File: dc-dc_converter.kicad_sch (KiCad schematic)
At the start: 11 parts

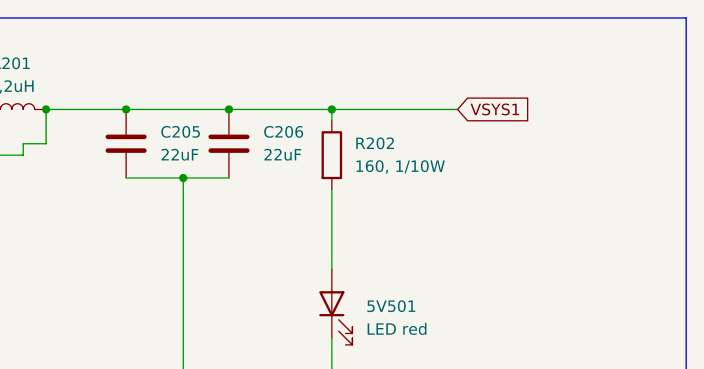
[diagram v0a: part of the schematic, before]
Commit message: daughterboard created
divided into mainboard and daughterboard
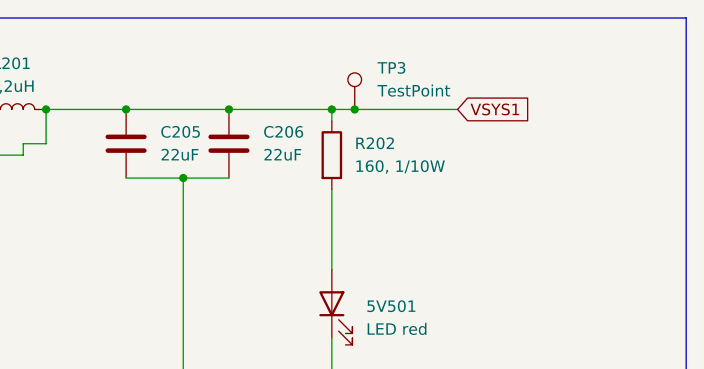
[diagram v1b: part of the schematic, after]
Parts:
- added TP3: TestPoint, TestPoint:TestPoint_Pad_D1.0mm, symbol Connector:TestPoint
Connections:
- net VSYS1: now also TP3.1
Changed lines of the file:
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@@
+	)
+	(junction
+		(at 200.66 39.37)
+		(diameter 0)
+		(color 0 0 0 0)
 	)
 	(junction
@@
 	(wire
 		(pts
+			(xy 200.66 39.37) (xy 212.09 39.37)
+		)
+		(stroke
+			(width 0)
+			(type default)
+		)
+	)
+	(wire
+		(pts
 			(xy 163.83 43.18) (xy 166.37 43.18)
 		)
@@
 	(wire
 		(pts
-			(xy 198.12 39.37) (xy 212.09 39.37)
+			(xy 198.12 39.37) (xy 200.66 39.37)
 		)
 		(stroke
@@
 					(unit 1)
 				)
+			)
+		)
+	)
+	(symbol
+		(lib_id "Connector:TestPoint")
+		(at 200.66 39.37 0)
+		(unit 1)
+		(exclude_from_sim no)
+		(in_bom yes)
+		(on_board yes)
+		(dnp no)
+		(fields_autoplaced yes)
+		(property "Reference" "TP3"
+			(at 203.2 34.7979 0)
+			(effects
+				(font
+					(size 1.27 1.27)
+				)
+				(justify left)
+			)
+		)
+		(property "Value" "TestPoint"
+			(at 203.2 37.3379 0)
+			(effects
+				(font
+					(size 1.27 1.27)
+				)
+				(justify left)
+			)
+		)
+		(property "Footprint" "TestPoint:TestPoint_Pad_D1.0mm"
+			(at 205.74 39.37 0)
+			(effects
+				(font
+					(size 1.27 1.27)
+				)
+				(hide yes)
+			)
+		)
+		(property "Datasheet" "~"
+			(at 205.74 39.37 0)
+			(effects
+				(font
+					(size 1.27 1.27)
+				)
+				(hide yes)
+			)
+		)
+		(property "Description" "test point"
+			(at 200.66 39.37 0)
+			(effects
+				(font
+					(size 1.27 1.27)
+				)
+				(hide yes)
+			)
+		)
+		(pin "1"
+		)
+		(instances
+			(project ""
+				(path "/63d8ebc3-d81d-4869-925f-b28ad884a523/58486cd9-8a71-4336-9353-75b232eb4196"
+					(reference "TP3")
+					(unit 1)
+				)
